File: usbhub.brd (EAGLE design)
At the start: 0 parts

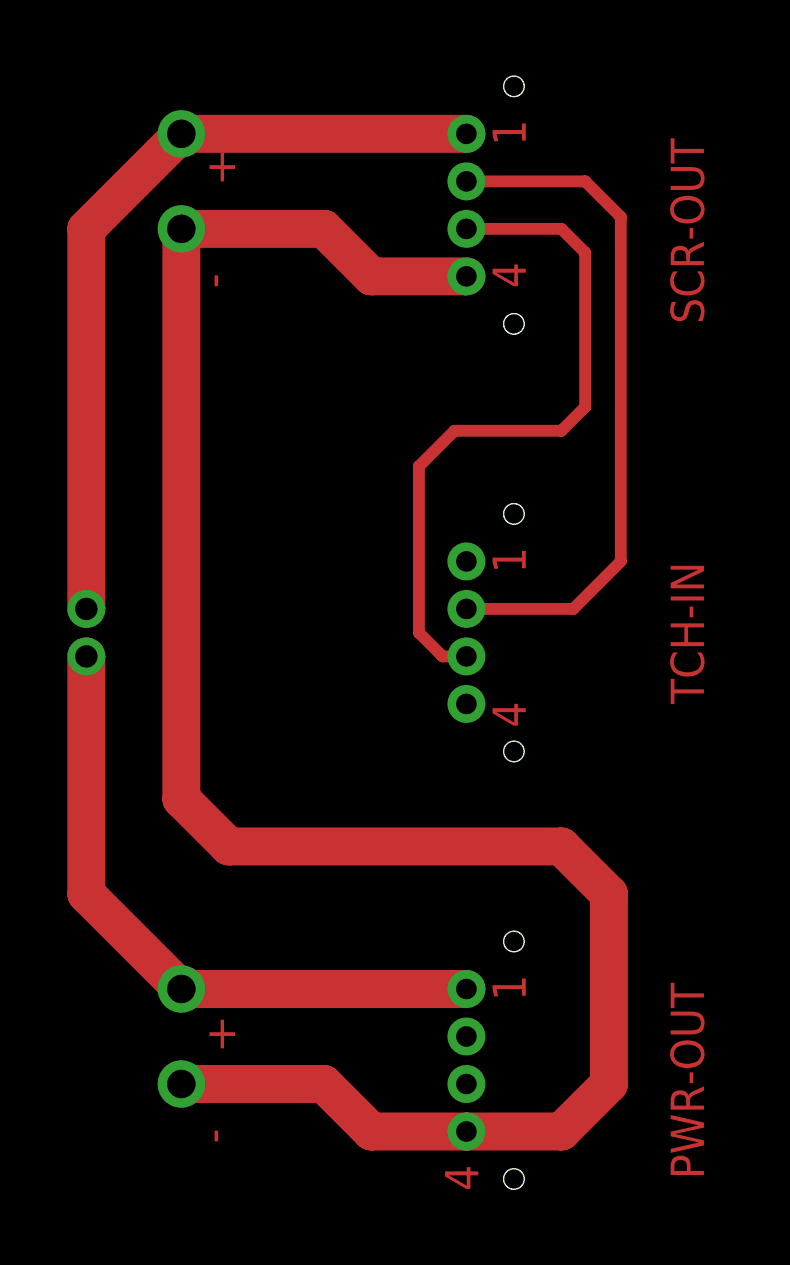
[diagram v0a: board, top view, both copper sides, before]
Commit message: Added dimensions and holes
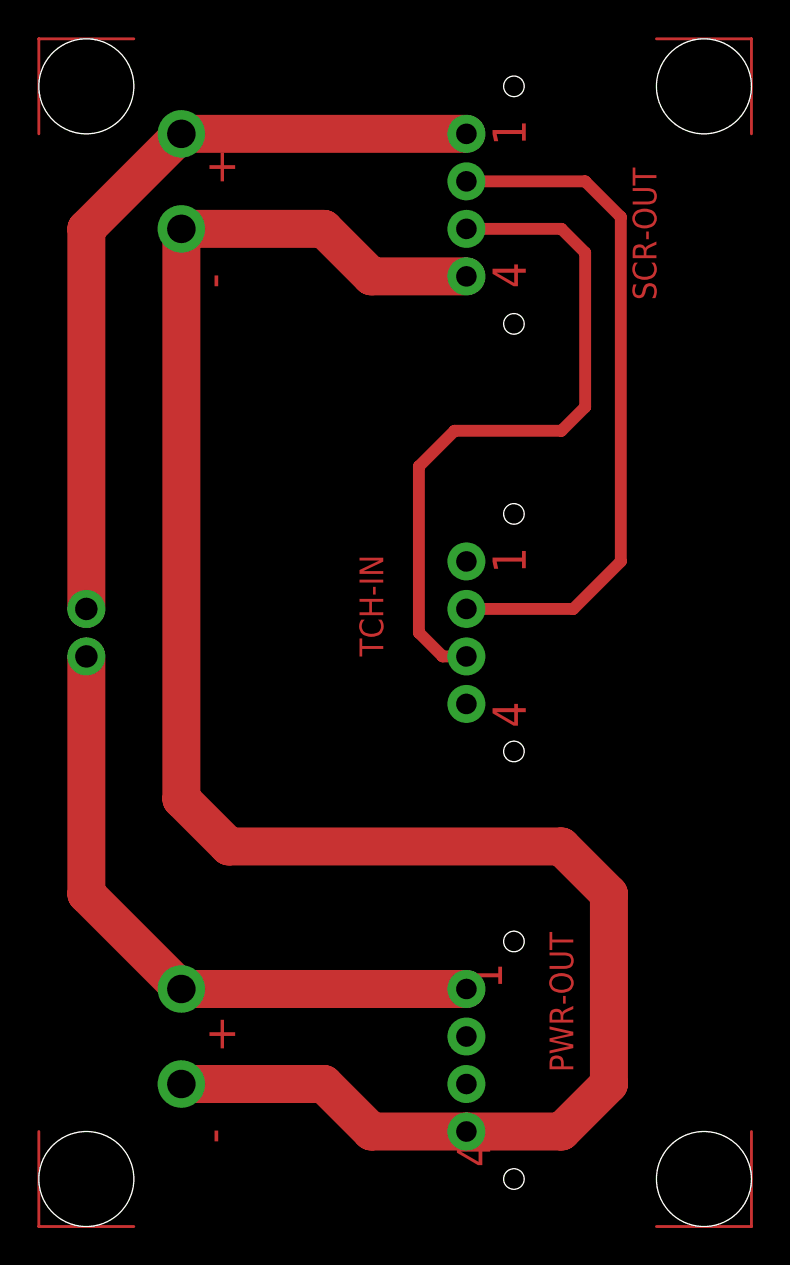
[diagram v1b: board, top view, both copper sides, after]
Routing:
- net S$13: track 0.00 -> 10.2 mm
- net S$1: track 0.00 -> 10.2 mm
- net S$10: track 0.00 -> 10.2 mm
- net S$5: track 0.00 -> 10.2 mm
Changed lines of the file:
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@@
 <?xml version="1.0" encoding="utf-8"?>
 <!DOCTYPE eagle SYSTEM "eagle.dtd">
-<eagle version="7.3.0">
+<eagle version="9.2.2">
 <drawing>
 <settings>
 <setting alwaysvectorfont="no"/>
+<setting keepoldvectorfont="yes"/>
 <setting verticaltext="up"/>
 </settings>
-<grid distance="25" unitdist="mil" unit="mil" style="lines" multiple="1" display="yes" altdistance="5" altunitdist="mil" altunit="mil"/>
+<grid distance="100" unitdist="mil" unit="mil" style="lines" multiple="1" display="yes" altdistance="5" altunitdist="mil" altunit="mil"/>
 <layers>
 <layer number="1" name="Top" color="4" fill="1" visible="yes" active="yes"/>
@@
 <hole x="50.8" y="7.62" drill="1.1"/>
 <hole x="50.8" y="20.32" drill="1.1"/>
-<text x="60.96" y="53.34" size="1.778" layer="1" rot="R90">SCR-OUT</text>
-<text x="60.96" y="33.02" size="1.778" layer="1" rot="R90">TCH-IN</text>
-<text x="60.96" y="7.62" size="1.778" layer="1" rot="R90">PWR-OUT</text>
+<text x="58.42" y="54.61" size="1.27" layer="1" font="vector" rot="R90">SCR-OUT</text>
+<text x="43.815" y="35.56" size="1.27" layer="1" font="vector" rot="R90">TCH-IN</text>
+<text x="53.975" y="13.335" size="1.27" layer="1" font="vector" rot="R90">PWR-OUT</text>
 <text x="34.29" y="60.96" size="1.778" layer="1" font="fixed">+</text>
 <text x="34.29" y="14.605" size="1.778" layer="1" font="fixed">+</text>
@@
 <text x="51.435" y="62.865" size="1.778" layer="1" font="fixed" rot="R90">1</text>
 <text x="51.435" y="40.005" size="1.778" layer="1" font="fixed" rot="R90">1</text>
-<text x="51.435" y="17.145" size="1.778" layer="1" font="fixed" rot="R90">1</text>
-<text x="48.895" y="6.985" size="1.778" layer="1" font="fixed" rot="R90">4</text>
+<text x="50.165" y="17.78" size="1.778" layer="1" font="fixed" rot="R90">1</text>
+<text x="49.53" y="8.255" size="1.778" layer="1" font="fixed" rot="R90">4</text>
 <text x="51.435" y="31.75" size="1.778" layer="1" font="fixed" rot="R90">4</text>
 <text x="51.435" y="55.245" size="1.778" layer="1" font="fixed" rot="R90">4</text>
+<hole x="27.94" y="7.62" drill="5.08"/>
+<hole x="60.96" y="66.04" drill="5.08"/>
+<hole x="27.94" y="66.04" drill="5.08"/>
+<hole x="60.96" y="7.62" drill="5.08"/>
+<dimension x1="63.5" y1="68.58" x2="63.5" y2="5.08" x3="76.2" y3="36.83" textsize="1.27" layer="1"/>
+<dimension x1="25.4" y1="5.08" x2="76.2" y2="5.08" x3="50.8" y3="-5.08" textsize="1.27" layer="1"/>
 </plain>
 <attributes>
@@
 <param name="dpMaxLengthDifference" value="10mm"/>
 <param name="dpGapFactor" value="2.5"/>
-<param name="checkGrid" value="0"/>
 <param name="checkAngle" value="0"/>
 <param name="checkFont" value="1"/>
 <param name="checkRestrict" value="1"/>
+<param name="checkStop" value="0"/>
+<param name="checkValues" value="0"/>
+<param name="checkNames" value="1"/>
+<param name="checkWireStubs" value="1"/>
+<param name="checkPolygonWidth" value="0"/>
 <param name="useDiameter" value="13"/>
 <param name="maxErrors" value="50"/>
@@
 <wire x1="33.02" y1="17.78" x2="48.26" y2="17.78" width="2.032" layer="1"/>
 </signal>
+<signal name="S$1">
+<wire x1="25.4" y1="68.58" x2="25.4" y2="63.5" width="0.1524" layer="1"/>
+<wire x1="30.48" y1="68.58" x2="25.4" y2="68.58" width="0.1524" layer="1"/>
+</signal>
+<signal name="S$5">
+<wire x1="58.42" y1="68.58" x2="63.5" y2="68.58" width="0.1524" layer="1"/>
+<wire x1="63.5" y1="68.58" x2="63.5" y2="63.5" width="0.1524" layer="1"/>
+</signal>
+<signal name="S$10">
+<wire x1="63.5" y1="10.16" x2="63.5" y2="5.08" width="0.1524" layer="1"/>
+<wire x1="63.5" y1="5.08" x2="58.42" y2="5.08" width="0.1524" layer="1"/>
+</signal>
+<signal name="S$13">
+<wire x1="25.4" y1="10.16" x2="25.4" y2="5.08" width="0.1524" layer="1"/>
+<wire x1="25.4" y1="5.08" x2="30.48" y2="5.08" width="0.1524" layer="1"/>
+</signal>
 </signals>
+<mfgpreviewcolors>
+<mfgpreviewcolor name="soldermaskcolor" color="0xC8008000"/>
+<mfgpreviewcolor name="silkscreencolor" color="0xFFFEFEFE"/>
+<mfgpreviewcolor name="backgroundcolor" color="0xFF282828"/>
+<mfgpreviewcolor name="coppercolor" color="0xFFFFBF00"/>
+<mfgpreviewcolor name="substratecolor" color="0xFF786E46"/>
+</mfgpreviewcolors>
 </board>
 </drawing>
